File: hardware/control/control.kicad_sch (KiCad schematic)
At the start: 58 parts, among them J1 Conn_01x05_Male, J2 CANPWR, J3 CANGND, J4 RJ45, J5 RJ45, J6 Conn_02x03_Odd_Even, Q1 BSS123, SW1 next, SW2 select, U1 2.048V, U2 AP63200WU, U3 PIC18F27Q84, U4 TLE9250VSJXUMA1, Y1 10Mhz

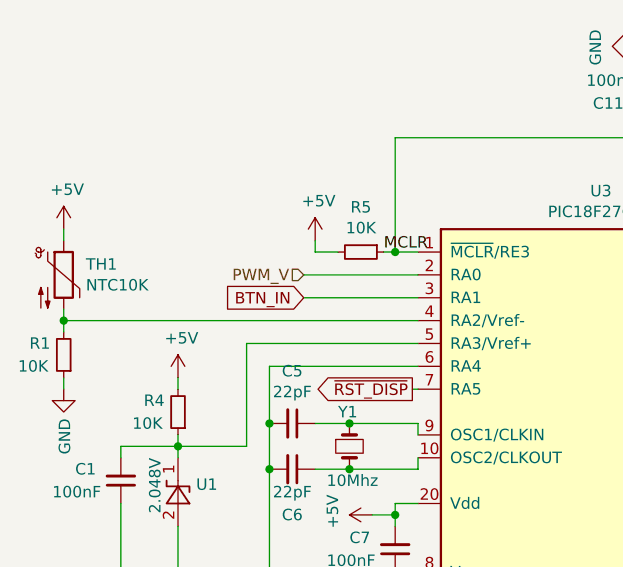
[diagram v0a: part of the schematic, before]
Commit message: Move thermistor to power-dcdc board (measure board temp) Adjust power-dcdc board layout, pass DRC
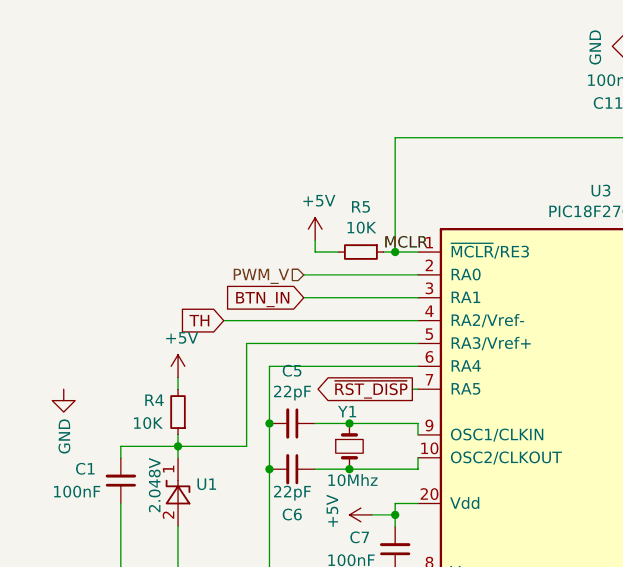
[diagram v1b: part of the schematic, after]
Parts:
- removed R1: 10K, Resistor_SMD:R_0805_2012Metric_Pad1.20x1.40mm_HandSolder, symbol Device:R_Small
- removed TH1: NTC10K, Resistor_SMD:R_0201_0603Metric_Pad0.64x0.40mm_HandSolder, symbol Device:Thermistor_NTC
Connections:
- net TH: now reaches U3.4 (RA2/Vref-)
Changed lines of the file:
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@@
   (junction (at 58.42 85.09) (diameter 0) (color 0 0 0 0)
-  )
-  (junction (at 21.59 57.15) (diameter 0) (color 0 0 0 0)
   )
   (junction (at 34.29 71.12) (diameter 0) (color 0 0 0 0)
@@
     (stroke (width 0) (type default) (color 0 0 0 0))
   )
-  (wire (pts (xy 21.59 48.26) (xy 21.59 46.99))
-    (stroke (width 0) (type default) (color 0 0 0 0))
-  )
   (wire (pts (xy 76.2 163.195) (xy 69.85 163.195))
     (stroke (width 0) (type default) (color 0 0 0 0))
@@
     (stroke (width 0) (type default) (color 0 0 0 0))
   )
+  (wire (pts (xy 39.37 57.15) (xy 60.96 57.15))
+    (stroke (width 0) (type default) (color 0 0 0 0))
+  )
   (wire (pts (xy 132.08 86.36) (xy 132.08 82.55))
     (stroke (width 0) (type default) (color 0 0 0 0))
@@
     (stroke (width 0) (type default) (color 0 0 0 0))
   )
-  (wire (pts (xy 21.59 57.15) (xy 21.59 55.88))
-    (stroke (width 0) (type default) (color 0 0 0 0))
-  )
   (wire (pts (xy 24.13 172.085) (xy 44.45 172.085))
     (stroke (width 0) (type default) (color 0 0 0 0))
@@
     (stroke (width 0) (type default) (color 0 0 0 0))
   )
-  (wire (pts (xy 21.59 58.42) (xy 21.59 57.15))
-    (stroke (width 0) (type default) (color 0 0 0 0))
-  )
   (wire (pts (xy 231.14 52.07) (xy 207.01 52.07))
     (stroke (width 0) (type default) (color 0 0 0 0))
@@
     (stroke (width 0) (type default) (color 0 0 0 0))
   )
-  (wire (pts (xy 21.59 57.15) (xy 60.96 57.15))
-    (stroke (width 0) (type default) (color 0 0 0 0))
-  )
   (wire (pts (xy 194.31 49.53) (xy 194.31 52.07))
     (stroke (width 0) (type default) (color 0 0 0 0))
@@
   )
   (wire (pts (xy 147.32 152.4) (xy 149.86 152.4))
-    (stroke (width 0) (type default) (color 0 0 0 0))
-  )
-  (wire (pts (xy 21.59 64.77) (xy 21.59 63.5))
     (stroke (width 0) (type default) (color 0 0 0 0))
   )
@@
     (property "Intersheet References" "${INTERSHEET_REFS}" (id 0) (at 141.8107 79.9306 0)
       (effects (font (size 1.27 1.27)) (justify left) hide)
+    )
+  )
+  (global_label "TH" (shape input) (at 39.37 57.15 180) (fields_autoplaced)
+    (effects (font (size 1.27 1.27)) (justify right))
+    (property "Intersheet References" "${INTERSHEET_REFS}" (id 0) (at 34.6588 57.0706 0)
+      (effects (font (size 1.27 1.27)) (justify right) hide)
     )
   )
@@
     (pin "2")
   )
-  (symbol (lib_id "Device:Thermistor_NTC") (at 21.59 52.07 0) (unit 1)
-    (in_bom yes) (on_board yes)
-    (property "Reference" "TH1" (id 0) (at 24.0538 50.9016 0)
-      (effects (font (size 1.27 1.27)) (justify left))
-    )
-    (property "Value" "NTC10K" (id 1) (at 24.0538 53.213 0)
-      (effects (font (size 1.27 1.27)) (justify left))
-    )
-    (property "Footprint" "Resistor_SMD:R_0201_0603Metric_Pad0.64x0.40mm_HandSolder" (id 2) (at 21.59 50.8 0)
-      (effects (font (size 1.27 1.27)) hide)
-    )
-    (property "Datasheet" "~" (id 3) (at 21.59 50.8 0)
-      (effects (font (size 1.27 1.27)) hide)
-    )
-    (property "P/N" " NT06104F3950B1H " (id 4) (at 21.59 52.07 0)
-      (effects (font (size 1.27 1.27)) hide)
-    )
-    (pin "1")
-    (pin "2")
-  )
-  (symbol (lib_id "Device:R_Small") (at 21.59 60.96 180) (unit 1)
-    (in_bom yes) (on_board yes)
-    (property "Reference" "R1" (id 0) (at 17.78 59.69 0)
-      (effects (font (size 1.27 1.27)) (justify right))
-    )
-    (property "Value" "10K" (id 1) (at 16.51 62.23 0)
-      (effects (font (size 1.27 1.27)) (justify right))
-    )
-    (property "Footprint" "Resistor_SMD:R_0805_2012Metric_Pad1.20x1.40mm_HandSolder" (id 2) (at 21.59 60.96 0)
-      (effects (font (size 1.27 1.27)) hide)
-    )
-    (property "Datasheet" "~" (id 3) (at 21.59 60.96 0)
-      (effects (font (size 1.27 1.27)) hide)
-    )
-    (pin "1")
-    (pin "2")
-  )
   (symbol (lib_id "power:GND") (at 36.83 136.525 90) (unit 1)
     (in_bom yes) (on_board yes) (fields_autoplaced)
@@
     (pin "1")
     (pin "2")
-  )
-  (symbol (lib_id "power:+5V") (at 21.59 46.99 0) (unit 1)
-    (in_bom yes) (on_board yes)
-    (property "Reference" "#PWR01" (id 0) (at 21.59 50.8 0)
-      (effects (font (size 1.27 1.27)) hide)
-    )
-    (property "Value" "+5V" (id 1) (at 21.971 42.5958 0))
-    (property "Footprint" "" (id 2) (at 21.59 46.99 0)
-      (effects (font (size 1.27 1.27)) hide)
-    )
-    (property "Datasheet" "" (id 3) (at 21.59 46.99 0)
-      (effects (font (size 1.27 1.27)) hide)
-    )
-    (pin "1")
   )
   (symbol (lib_id "Diode:1.5KExxA") (at 201.93 53.34 90) (unit 1)
@@
       (reference "#FLG02") (unit 1) (value "PWR_FLAG") (footprint "")
     )
-    (path "/d3736b6e-dd53-4201-9eef-925312bed583"
-      (reference "#PWR01") (unit 1) (value "+5V") (footprint "")
-    )
     (path "/3e10e71c-07e7-4da7-b50e-cf273ebe2503"
       (reference "#PWR02") (unit 1) (value "GND") (footprint "")
@@
       (reference "Q1") (unit 1) (value "BSS123") (footprint "Package_TO_SOT_SMD:SOT-23")
     )
-    (path "/846532de-7e53-4790-a259-17d902b2f08e"
-      (reference "R1") (unit 1) (value "10K") (footprint "Resistor_SMD:R_0805_2012Metric_Pad1.20x1.40mm_HandSolder")
-    )
     (path "/e4041874-f83b-4e5a-ae56-4761689b06b4"
       (reference "R2") (unit 1) (value "270k") (footprint "Resistor_SMD:R_0805_2012Metric_Pad1.20x1.40mm_HandSolder")
@@
       (reference "SW2") (unit 1) (value "select") (footprint "Button_Switch_THT:Push_E-Switch_KS01Q01")
     )
-    (path "/81ac232b-00a5-466f-8c6e-5111f94b53c2"
-      (reference "TH1") (unit 1) (value "NTC10K") (footprint "Resistor_SMD:R_0201_0603Metric_Pad0.64x0.40mm_HandSolder")
-    )
     (path "/9f51c40e-e3e0-4350-85ba-c63293d5dcc2"

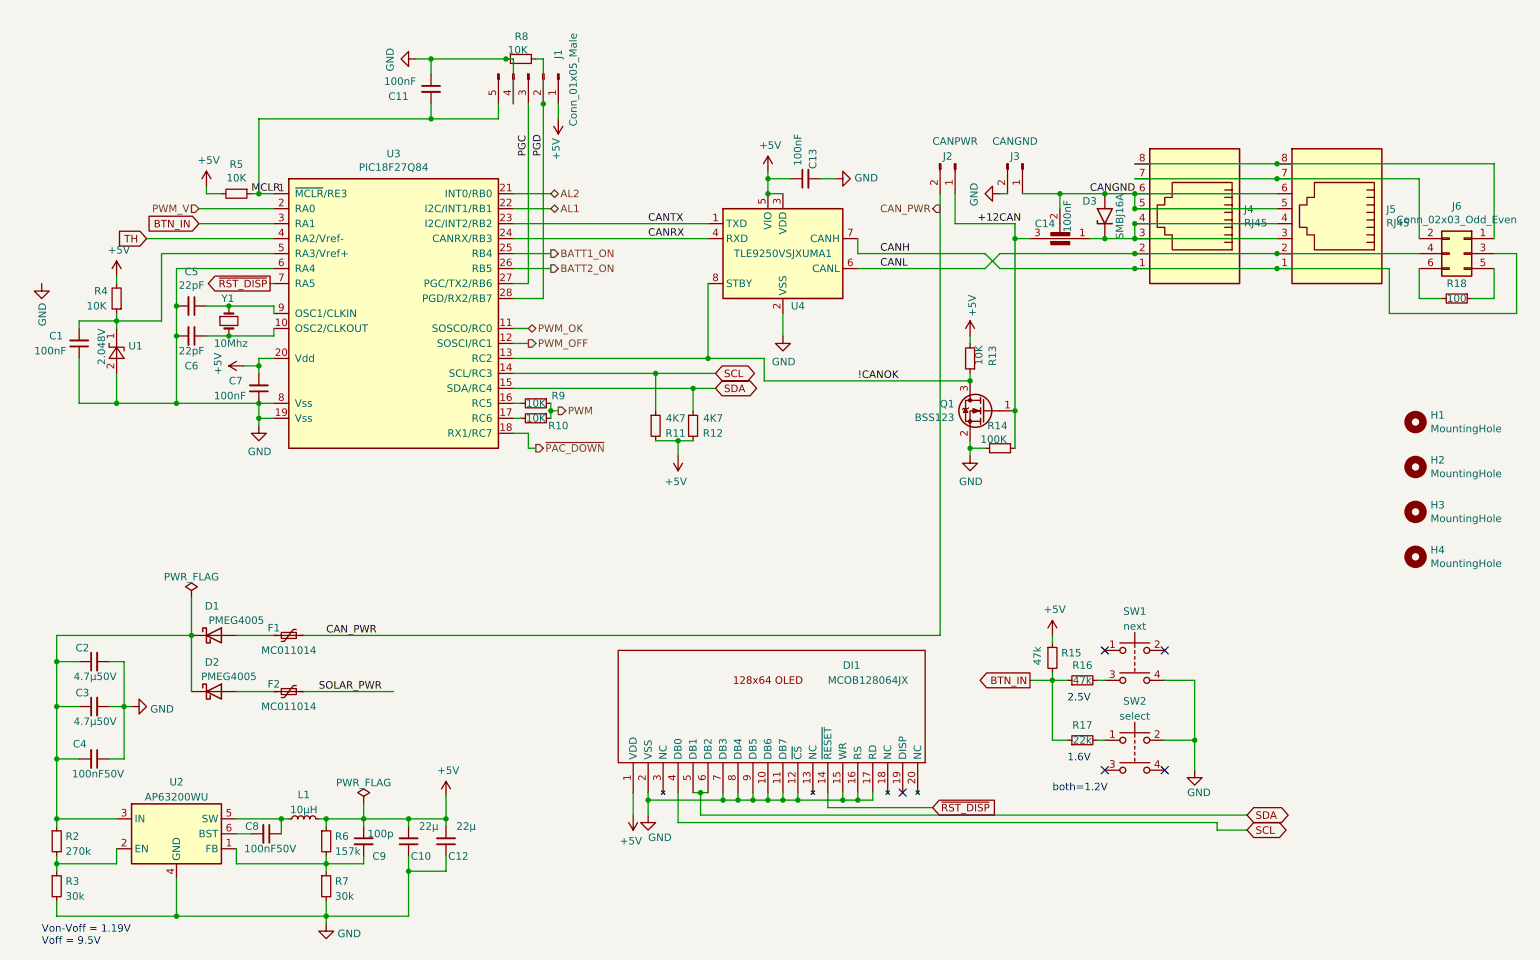
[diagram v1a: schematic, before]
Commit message: Add board-to-board connectors in control schematic
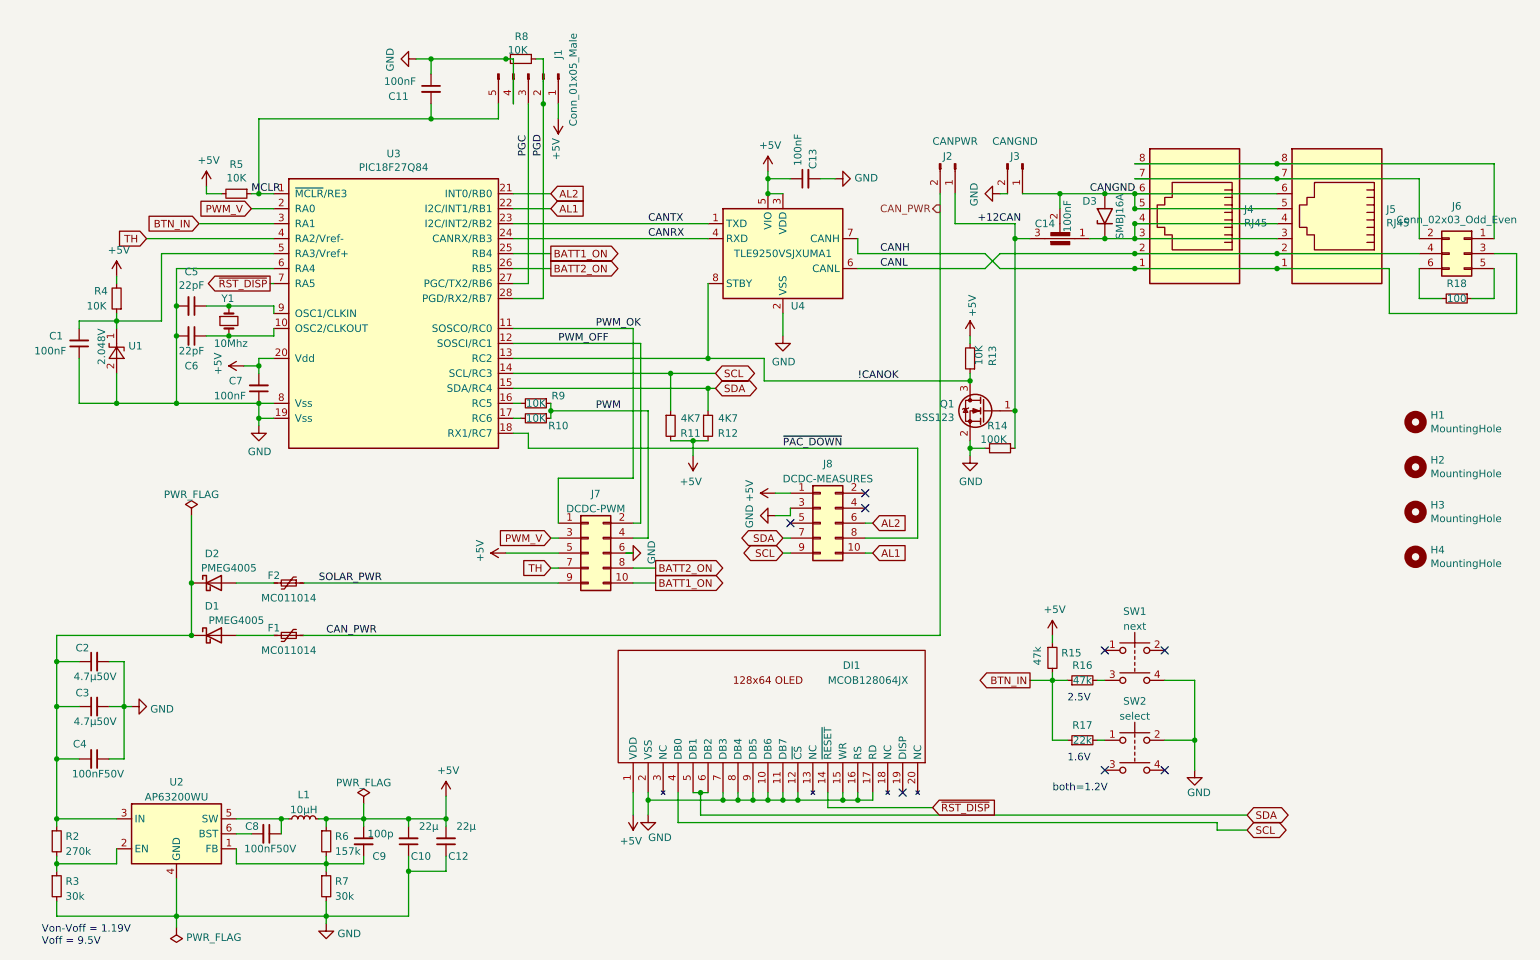
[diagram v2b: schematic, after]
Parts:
- added J7: DCDC-PWM, Connector_PinHeader_2.54mm:PinHeader_2x05_P2.54mm_Vertical, symbol Connector_Generic:Conn_02x05_Odd_Even
- added J8: DCDC-MEASURES, Connector_PinHeader_2.54mm:PinHeader_2x05_P2.54mm_Vertical, symbol Connector_Generic:Conn_02x05_Odd_Even
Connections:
- net +5V: now also J7.5 (Pin_5), J8.1 (Pin_1)
- net AL1: now also J8.10 (Pin_10)
- net AL2: now also J8.6 (Pin_6)
- net BATT1_ON: now also J7.10 (Pin_10)
- net BATT2_ON: now also J7.8 (Pin_8)
- net GND: now also J7.6 (Pin_6), J8.3 (Pin_3)
- net PWM: now also J7.4 (Pin_4)
- net PWM_OFF: now also J7.2 (Pin_2)
- net PWM_OK: now also J7.1 (Pin_1)
- net PWM_V: now also J7.3 (Pin_3)
- net SCL: now also J8.9 (Pin_9)
- net SDA: now also J8.7 (Pin_7)
- net SOLAR_PWR: now also J7.9 (Pin_9)
- net TH: now also J7.7 (Pin_7)
- net ~{PAC_DOWN}: now also J8.8 (Pin_8)
- no-connect marks 5 -> 8
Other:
- moved on the sheet: D2, F2, R11, R12
